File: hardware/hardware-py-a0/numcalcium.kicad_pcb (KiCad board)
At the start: 2 copper layers, 77.6 x 158.1 mm, 111 parts, among them J1 Conn_02x08_Odd_Even, J12 Micro_SD_Card_Det2, J2 USB_C_Receptacle_USB2.0_16P, J3 Conn_02x04_Odd_Even, J4 LCD_socket, J9 AudioJack4, Q1 AO3401A, Q2 AO3401A, Q3 AO3401A, Q6 BSS138, Q7 AO3401A, Q8 BSS138, Q9 BSS138, SW1 SW_Push, SW10 SW_Push, SW11 SW_Push, SW12 SW_Push, SW13 SW_Push, SW14 SW_Push, SW15 SW_Push, SW16 SW_Push, SW17 SW_Push, SW18 SW_Push, SW19 SW_Push, SW2 SW_Push, SW20 SW_Push, SW21 Encoder, SW22 RST, SW3 SW_Push, SW4 SW_Push, SW5 SW_Push, SW6 SW_Push, SW7 SW_Push, SW8 SW_Push, SW9 SW_Push, U1 LTC4054ES5-4.2, U2 STI3411A, U3 74HC595, U4 ESP32-S3-WROOM-1, U6 XC6206PxxxMR

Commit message: [dev] py-a0 board files
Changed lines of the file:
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@@
 		(tags "SOT TO_SOT_SMD")
 		(property "Reference" "U6"
-			(at -0.508 0 360)
+			(at -0.508 0 0)
 			(layer "F.SilkS")
 			(effects
@@
 		)
 		(property "Value" "XC6206PxxxMR"
-			(at 0 2.4 360)
+			(at 0 2.4 0)
 			(layer "F.Fab")
 			(effects
@@
 		)
 		(fp_text user "${REFERENCE}"
-			(at 0 0 360)
+			(at 0 0 0)
 			(layer "F.Fab")
 			(effects
@@
 		(tags "diode handsolder")
 		(property "Reference" "D24"
-			(at -0.009 0.0254 360)
+			(at -0.009 0.0254 0)
 			(layer "F.SilkS")
 			(effects
@@
 		(tags "SOT TO_SOT_SMD")
 		(property "Reference" "Q3"
-			(at -0.6835 0 360)
+			(at -0.6835 0 0)
 			(layer "F.SilkS")
 			(effects
@@
 		)
 		(property "Value" "AO3401A"
-			(at 0 2.4 360)
+			(at 0 2.4 0)
 			(layer "F.Fab")
 			(effects
@@
 		)
 		(fp_text user "${REFERENCE}"
-			(at 0 0 360)
+			(at 0 0 0)
 			(layer "F.Fab")
 			(effects
@@
 		)
 		(fp_text user "+"
-			(at -1.326 4.9836 360)
+			(at -1.326 4.9836 0)
 			(layer "B.SilkS")
 			(effects
@@
 		)
 		(fp_text user "+"
-			(at -2.75 2.75 360)
+			(at -2.75 2.75 0)
 			(layer "B.Fab")
 			(effects
@@
 		(tags "diode handsolder")
 		(property "Reference" "D27"
-			(at 0 -0.0254 360)
+			(at 0 -0.0254 0)
 			(layer "B.SilkS")
 			(effects
@@
 		(polygon
 			(pts
-				(xy -1.016 -35.56) (xy 33.528 -35.56) (xy 33.528 -27.432) (xy 57.912 -27.432) (xy 57.912 -3.048)
+				(xy -1.2192 -35.6108) (xy 33.528 -35.56) (xy 33.528 -27.432) (xy 57.912 -27.432) (xy 57.912 -3.048)
 				(xy -1.016 -3.048)
 			)

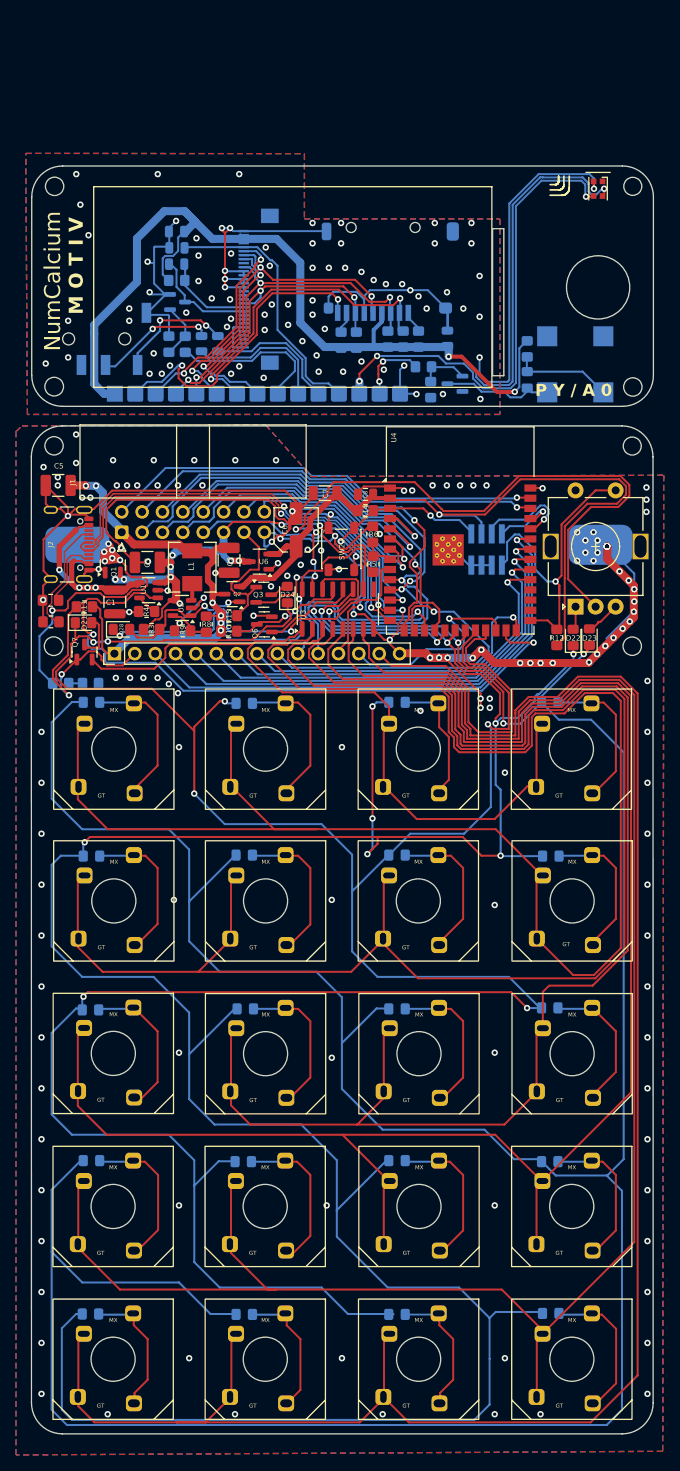
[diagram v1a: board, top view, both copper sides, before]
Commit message: hardware: py/a0 revision 1.1 using FFC connectors
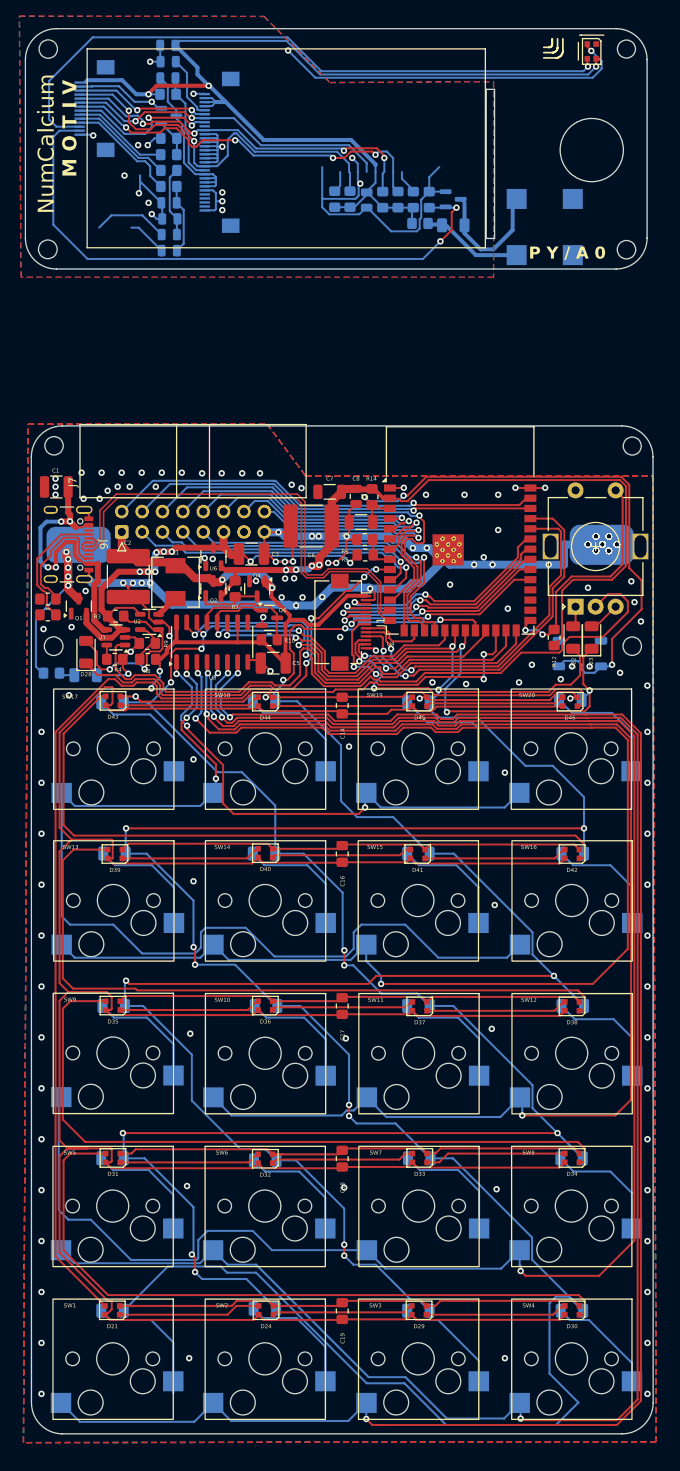
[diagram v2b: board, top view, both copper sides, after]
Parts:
- removed IPC1: Conn_01x16_Pin, Connector_PinHeader_2.54mm:PinHeader_1x15_P2.54mm_Vertical
- removed IPC2: Conn_01x16_Socket, footprints:PinSocket_1x15_P2.54mm_Vertical_Pads
- removed J12: Micro_SD_Card_Det2, footprints:microSD_Short_1
- removed J4: LCD_socket, Connector_FFC-FPC:Hirose_FH12-30S-0.5SH_1x30-1MP_P0.50mm_Horizontal
- removed J9: AudioJack4, footprints:Jack_3.5mm_PJ320D_Horizontal
- removed Q3, Q7: AO3401A, Package_TO_SOT_SMD:SOT-23
- removed R15: 100k, Resistor_SMD:R_0805_2012Metric_Pad1.20x1.40mm_HandSolder
- added C14: 1u, Capacitor_SMD:C_0805_2012Metric_Pad1.18x1.45mm_HandSolder, F.Cu at (38.2, 33.3)
- added C16: 1u, Capacitor_SMD:C_0805_2012Metric_Pad1.18x1.45mm_HandSolder, F.Cu at (38.2, 51.8)
- added C17: 1u, Capacitor_SMD:C_0805_2012Metric_Pad1.18x1.45mm_HandSolder, F.Cu at (38.2, 70.7)
- added C18: 1u, Capacitor_SMD:C_0805_2012Metric_Pad1.18x1.45mm_HandSolder, F.Cu at (38.2, 89.8)
- added C19: 1u, Capacitor_SMD:C_0805_2012Metric_Pad1.18x1.45mm_HandSolder, F.Cu at (38.2, 108.8)
- added C20: 470n, Capacitor_SMD:C_0805_2012Metric, B.Cu at (16.7, -27.4)
- added C21: 470n, Capacitor_SMD:C_0805_2012Metric, B.Cu at (16.6, -29.4)
- added C4: 1u, Capacitor_SMD:C_1206_3216Metric, F.Cu at (40.6, 10.4)
- added D29: WS2812B-2020, LED_SMD:LED_WS2812B-2020_PLCC4_2.0x2.0mm, F.Cu at (47.8, 108.7)
- added D30: WS2812B-2020, LED_SMD:LED_WS2812B-2020_PLCC4_2.0x2.0mm, F.Cu at (66.9, 108.7)
- added D31: WS2812B-2020, LED_SMD:LED_WS2812B-2020_PLCC4_2.0x2.0mm, F.Cu at (9.66, 89.7)
- added D32: WS2812B-2020, LED_SMD:LED_WS2812B-2020_PLCC4_2.0x2.0mm, F.Cu at (28.7, 89.8)
- added D33: WS2812B-2020, LED_SMD:LED_WS2812B-2020_PLCC4_2.0x2.0mm, F.Cu at (47.9, 89.7)
- added D34: WS2812B-2020, LED_SMD:LED_WS2812B-2020_PLCC4_2.0x2.0mm, F.Cu at (66.9, 89.7)
- added D35: WS2812B-2020, LED_SMD:LED_WS2812B-2020_PLCC4_2.0x2.0mm, F.Cu at (9.66, 70.7)
- added D36: WS2812B-2020, LED_SMD:LED_WS2812B-2020_PLCC4_2.0x2.0mm, F.Cu at (28.7, 70.7)
- added D37: WS2812B-2020, LED_SMD:LED_WS2812B-2020_PLCC4_2.0x2.0mm, F.Cu at (47.9, 70.8)
- added D38: WS2812B-2020, LED_SMD:LED_WS2812B-2020_PLCC4_2.0x2.0mm, F.Cu at (66.9, 70.8)
- added D39: WS2812B-2020, LED_SMD:LED_WS2812B-2020_PLCC4_2.0x2.0mm, F.Cu at (9.91, 51.8)
- added D40: WS2812B-2020, LED_SMD:LED_WS2812B-2020_PLCC4_2.0x2.0mm, F.Cu at (28.7, 51.7)
- added D41: WS2812B-2020, LED_SMD:LED_WS2812B-2020_PLCC4_2.0x2.0mm, F.Cu at (47.7, 51.8)
- added D42: WS2812B-2020, LED_SMD:LED_WS2812B-2020_PLCC4_2.0x2.0mm, F.Cu at (66.9, 51.8)
- added D43: WS2812B-2020, LED_SMD:LED_WS2812B-2020_PLCC4_2.0x2.0mm, F.Cu at (9.66, 32.7)
- added D44: WS2812B-2020, LED_SMD:LED_WS2812B-2020_PLCC4_2.0x2.0mm, F.Cu at (28.7, 32.8)
- added D45: WS2812B-2020, LED_SMD:LED_WS2812B-2020_PLCC4_2.0x2.0mm, F.Cu at (47.9, 32.8)
- added D46: WS2812B-2020, LED_SMD:LED_WS2812B-2020_PLCC4_2.0x2.0mm, F.Cu at (66.7, 32.8)
- added J6: USB_C_Receptacle_USB2.0_16P, Connector_USB:USB_C_Receptacle_GCT_USB4105-xx-A_16P_TopMnt_Horizontal, F.Cu at (2.97, 13.2)
- added J7: Conn_02x08_Odd_Even, footprints:IDC-Header_2x08_P2.54mm_Horizontal, F.Cu at (10.8, 11.6)
- added Q4: BSS138, Package_TO_SOT_SMD:SOT-23, F.Cu at (27.6, 18.7)
- added R7: 1M, Resistor_SMD:R_0805_2012Metric_Pad1.20x1.40mm_HandSolder, F.Cu at (24.9, 18.7)
- C2: value 22u -> 220u; footprint Resistor_SMD:R_1210_3225Metric_Pad1.30x2.65mm_HandSolder -> Capacitor_SMD:C_2220_5750Metric
- C6: footprint Capacitor_SMD:C_Elec_5x5.4 -> Capacitor_SMD:C_2220_5750Metric
- D1, D10, D11, D12, D13, D14, D15, D16, D17, D18, D19, D2, D20, D22, D23, D27, D28, D3, D4, D5, D6, D7, D8, D9: footprint Diode_SMD:D_0805_2012Metric_Pad1.15x1.40mm_HandSolder -> Diode_SMD:D_1206_3216Metric
- D21, D24: value D -> WS2812B-2020; footprint Diode_SMD:D_0805_2012Metric_Pad1.15x1.40mm_HandSolder -> LED_SMD:LED_WS2812B-2020_PLCC4_2.0x2.0mm
- D25: footprint Resistor_SMD:R_0805_2012Metric_Pad1.20x1.40mm_HandSolder -> Diode_SMD:D_1206_3216Metric
- J1: value Conn_02x08_Odd_Even -> Conn_01x14_Socket; footprint footprints:IDC-Header_2x08_P2.54mm_Horizontal -> Connector_FFC-FPC:Hirose_FH12-14S-0.5SH_1x14-1MP_P0.50mm_Horizontal
- J2: value USB_C_Receptacle_USB2.0_16P -> Conn_01x14_Socket; footprint Connector_USB:USB_C_Receptacle_GCT_USB4105-xx-A_16P_TopMnt_Horizontal -> Connector_FFC-FPC:Hirose_FH12-14S-0.5SH_1x14-1MP_P0.50mm_Horizontal; moved to B.Cu
- J3: value Conn_02x04_Odd_Even -> LCD_socket; footprint Connector_PinHeader_1.27mm:PinHeader_2x04_P1.27mm_Vertical_SMD -> Connector_FFC-FPC:Hirose_FH12-30S-0.5SH_1x30-1MP_P0.50mm_Horizontal
- R10: value 100k -> 1M
- R11: value 100k -> 100; moved to B.Cu
- R12: value 100k -> 470k
- R13: value 10k -> 100
- R14: value 100k -> 10k
- R16, R17: value 5k6 -> 5k1
- R27: value 10k -> 1M
- SW1, SW10, SW11, SW12, SW13, SW14, SW15, SW16, SW17, SW18, SW19, SW2, SW20, SW3, SW4, SW5, SW6, SW7, SW8, SW9: footprint footprints:Combo_MechanicalSwitch -> footprints:CherrySocket_MechanicalSwitch
- SW22: value RST -> SW_Push; moved to B.Cu
- moved D24 89.3 mm to (28.7, 108.7), turned to 180 degrees
- moved D21 85.8 mm to (9.58, 108.7), turned to 180 degrees
- moved J3 59.7 mm to (22.9, -35.7), turned to -90 degrees
- moved J2 54.5 mm to (7.34, -41.2)
- moved R11 53.5 mm to (16.6, -31.5)
- moved R13 40.1 mm to (16.6, -33.5), turned to 180 degrees
- moved C5 34.8 mm to (29.6, 28.0)
- moved SW22 32.5 mm to (67.9, 26.8), turned to 0 degrees
- moved J1 30.7 mm to (39.3, 22.9), turned to -90 degrees
- moved R18 25.7 mm to (16.6, -37.5), turned to 180 degrees
- moved R20 23.7 mm to (16.6, -35.4), turned to 0 degrees
- moved R27 23.7 mm to (49.1, -29.8), turned to 90 degrees
- moved C11 23.2 mm to (16.5, -47.0)
- moved Q9 23.2 mm to (16.6, -40.3)
- moved R19 23.2 mm to (16.5, -43.0)
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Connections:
- C12 pad 2: /Front/A_T -> Net-(C12-Pad2)
- C13 pad 2: /Front/A_R1 -> Net-(C13-Pad2)
- C9 pad 1: Net-(J4-Pin_21) -> Net-(J3-Pin_21)
- C9 pad 2: Net-(J4-Pin_20) -> Net-(J3-Pin_20)
- D21 pad 1: IO_T -> Net-(D21-DOUT)
- D21 pad 2: Net-(D21-A) -> GND
- D24 pad 1: IO_T -> Net-(D24-DOUT)
- D24 pad 2: Net-(D24-A) -> GND
- J1 pad 10: Net-(J1-Pin_10) -> /Main/AUD_R
- J1 pad 11: VBAT -> /Main/AUD_L
- J1 pad 12: Net-(J1-Pin_12) -> /Main/STATUS_LED
- J1 pad 13: CART_SENSE -> /Main/BUZ_DRIVE
- J1 pad 14: Net-(J1-Pin_14) -> GND
- J1 pad 2: Net-(J1-Pin_2) -> GND
- J1 pad 3: RX1 -> /Main/LCD_CS
- J1 pad 4: Net-(J1-Pin_4) -> /Main/MISO
- J1 pad 5: TX1 -> /Main/MOSI
- J1 pad 6: Net-(J1-Pin_6) -> /Main/CK
- J1 pad 7: Net-(J1-Pin_7) -> /Main/SD_CS
- J1 pad 8: Net-(J1-Pin_8) -> /Main/LCD_DC
- J1 pad 9: Net-(J1-Pin_9) -> /Main/LCD_LED
- J3 pad 1: #B_OK -> GND
- J3 pad 2: Net-(J3-Pin_2) -> /Front/VDD
- J3 pad 3: GND -> /Front/VDD
- J3 pad 4: Net-(J3-Pin_4) -> /Front/VDD
- J3 pad 5: GND -> /Front/LCD_RST
- J3 pad 6: VDD_AON -> /Front/LCD_CS
- J3 pad 7: GND -> /Front/CK
- J3 pad 8: RST -> /Front/LCD_DC
- Q2 pad 1: Net-(D28-A) -> Net-(Q2-G)
- Q8 pad 1: Net-(Q8-G) -> /Front/BUZZER
- Q9 pad 3: Net-(J4-Pin_21) -> Net-(J3-Pin_21)
- R11 pad 1: VDD -> Net-(C12-Pad2)
- R11 pad 2: /Main/SD_DET -> /Front/A_T
- R13 pad 1: /Front/BUZZER -> Net-(C13-Pad2)
- R13 pad 2: Net-(Q8-G) -> /Front/A_R1
- R14 pad 1: RST -> VDD_AON
- R14 pad 2: VDD_AON -> RST
- R16 pad 1: Net-(J2-CC2) -> Net-(J6-CC2)
- R17 pad 1: Net-(J2-CC1) -> Net-(J6-CC1)
- R19 pad 1: Net-(J4-Pin_20) -> Net-(J3-Pin_20)
- R27 pad 1: Net-(Q8-G) -> /Front/BUZZER
- SW1 pad 1: Net-(D1-A) -> Net-(U3-QH)
- SW1 pad 2: Net-(U3-QH) -> Net-(D1-A)
- SW10 pad 1: Net-(D10-A) -> Net-(U3-QE)
- SW10 pad 2: Net-(U3-QE) -> Net-(D10-A)
- SW11 pad 1: Net-(D11-A) -> Net-(U3-QE)
- SW11 pad 2: Net-(U3-QE) -> Net-(D11-A)
- SW12 pad 1: Net-(D12-A) -> Net-(U3-QE)
- SW12 pad 2: Net-(U3-QE) -> Net-(D12-A)
- SW13 pad 1: Net-(D13-A) -> Net-(U3-QD)
- SW13 pad 2: Net-(U3-QD) -> Net-(D13-A)
- SW14 pad 1: Net-(D14-A) -> Net-(U3-QD)
- SW14 pad 2: Net-(U3-QD) -> Net-(D14-A)
- SW15 pad 1: Net-(D15-A) -> Net-(U3-QD)
- SW15 pad 2: Net-(U3-QD) -> Net-(D15-A)
- SW16 pad 1: Net-(D16-A) -> Net-(U3-QC)
- SW16 pad 2: Net-(U3-QC) -> Net-(D16-A)
- SW17 pad 1: Net-(D17-A) -> Net-(U3-QC)
- SW17 pad 2: Net-(U3-QC) -> Net-(D17-A)
- SW18 pad 1: Net-(D18-A) -> Net-(U3-QC)
- SW18 pad 2: Net-(U3-QC) -> Net-(D18-A)
- SW19 pad 1: Net-(D19-A) -> Net-(U3-QB)
- SW19 pad 2: Net-(Q7-S) -> Net-(D19-A)
- SW2 pad 1: Net-(D2-A) -> Net-(U3-QH)
- SW2 pad 2: Net-(U3-QH) -> Net-(D2-A)
- SW20 pad 1: Net-(D20-A) -> Net-(U3-QB)
- SW20 pad 2: Net-(Q7-S) -> Net-(D20-A)
- SW3 pad 1: Net-(D3-A) -> Net-(U3-QH)
- SW3 pad 2: Net-(U3-QH) -> Net-(D3-A)
- SW4 pad 1: Net-(D4-A) -> Net-(U3-QG)
- SW4 pad 2: Net-(U3-QG) -> Net-(D4-A)
- SW5 pad 1: Net-(D5-A) -> Net-(U3-QG)
- SW5 pad 2: Net-(U3-QG) -> Net-(D5-A)
- SW6 pad 1: Net-(D6-A) -> Net-(U3-QG)
- SW6 pad 2: Net-(U3-QG) -> Net-(D6-A)
- SW7 pad 1: Net-(D7-A) -> Net-(U3-QF)
- SW7 pad 2: Net-(U3-QF) -> Net-(D7-A)
- SW8 pad 1: Net-(D8-A) -> Net-(U3-QF)
- SW8 pad 2: Net-(U3-QF) -> Net-(D8-A)
- SW9 pad 1: Net-(D9-A) -> Net-(U3-QF)
- SW9 pad 2: Net-(U3-QF) -> Net-(D9-A)
- U3 pad 1: Net-(Q7-S) -> Net-(U3-QB)
- U4 pad 12: Net-(J1-Pin_16) -> Net-(J7-Pin_16)
- U4 pad 15: Net-(J1-Pin_6) -> Net-(J7-Pin_6)
- U4 pad 17: Net-(J1-Pin_9) -> Net-(J7-Pin_9)
- U4 pad 18: Net-(J1-Pin_7) -> Net-(J7-Pin_7)
- U4 pad 24: /Main/STATUS_LED -> /Main/lighting/DIN
- U4 pad 36: Net-(J3-Pin_4) -> /Main/AUD_R
- U4 pad 37: Net-(J3-Pin_2) -> /Main/AUD_L
- U4 pad 38: Net-(J1-Pin_4) -> Net-(J7-Pin_4)
- U4 pad 39: Net-(J1-Pin_2) -> Net-(J7-Pin_2)
- U4 pad 4: Net-(J1-Pin_8) -> Net-(J7-Pin_8)
- U4 pad 5: Net-(J1-Pin_10) -> Net-(J7-Pin_10)
- U4 pad 6: Net-(J1-Pin_12) -> Net-(J7-Pin_12)
- U4 pad 7: Net-(J1-Pin_14) -> Net-(J7-Pin_14)
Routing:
- net VDD: track 97.8 -> 491.7 mm, vias 7 -> 4
- net GND: track 420.8 -> 605.2 mm, vias 240 -> 257
- net IO_D: track 421.8 -> 275.7 mm, vias 4 -> 13
- net /Main/lighting/DIN: track 0.00 -> 141.3 mm, vias 0 -> 2
- net IO_T: track 328.5 -> 213.6 mm
- net Net-(Q7-S): track 92.4 -> 0.00 mm
- net Net-(D38-DOUT): track 0.00 -> 89.2 mm
- net Net-(D34-DOUT): track 0.00 -> 88.4 mm
- net Net-(U3-QC): track 211.3 -> 123.4 mm, vias 0 -> 3
- net Net-(D42-DOUT): track 0.00 -> 86.9 mm
- net Net-(D30-DOUT): track 0.00 -> 86.8 mm
- net /Front/BUZZER: track 9.42 -> 74.1 mm
- net Net-(U3-QB): track 0.00 -> 61.9 mm, vias 0 -> 3
- net Net-(J1-Pin_2): track 54.9 -> 0.00 mm, vias 1 -> 0
- net Net-(J7-Pin_2): track 0.00 -> 54.5 mm, vias 0 -> 1
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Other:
- board size 77.6 x 158.1 mm -> 78.3 x 175.2 mm
- board text removed: "PROG"
- board text removed: "TRVR BGGG"

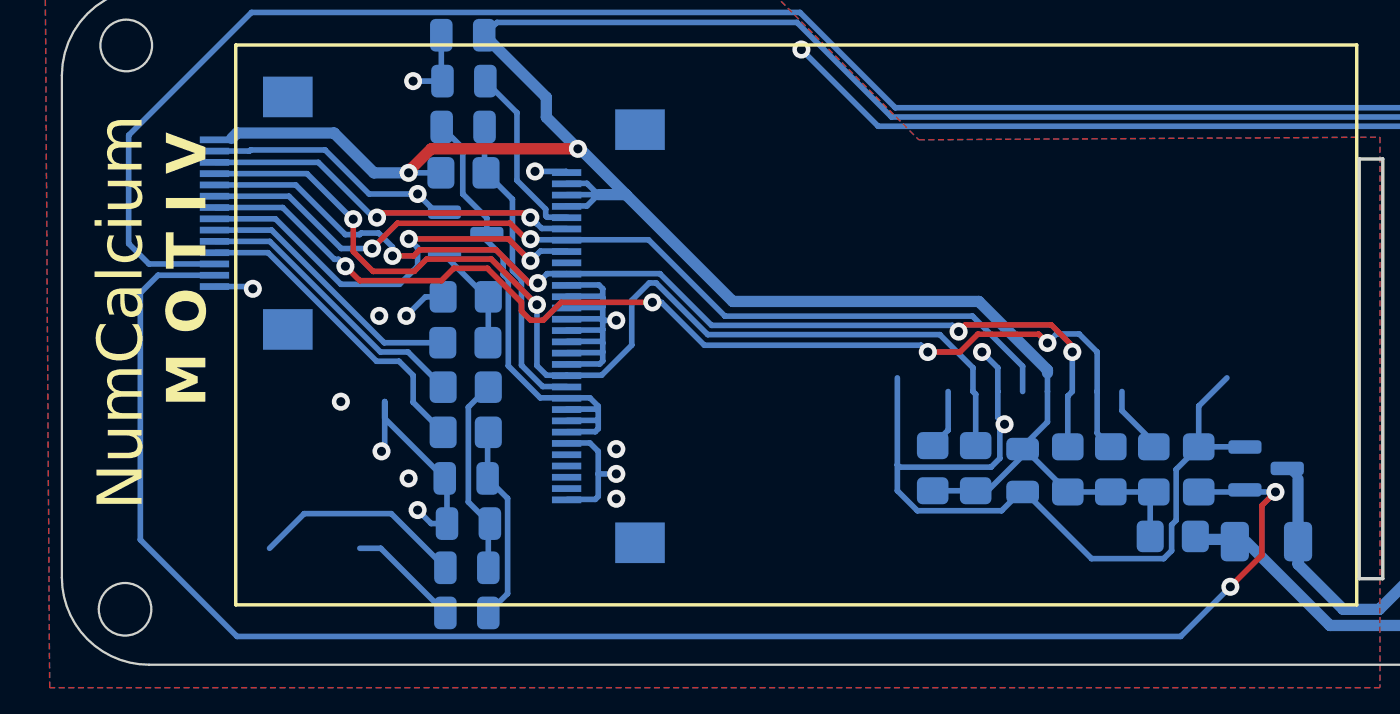
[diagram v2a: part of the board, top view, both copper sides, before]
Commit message: terminal:os.dupterm Stream support
move files and rename folders to board_src and scripts
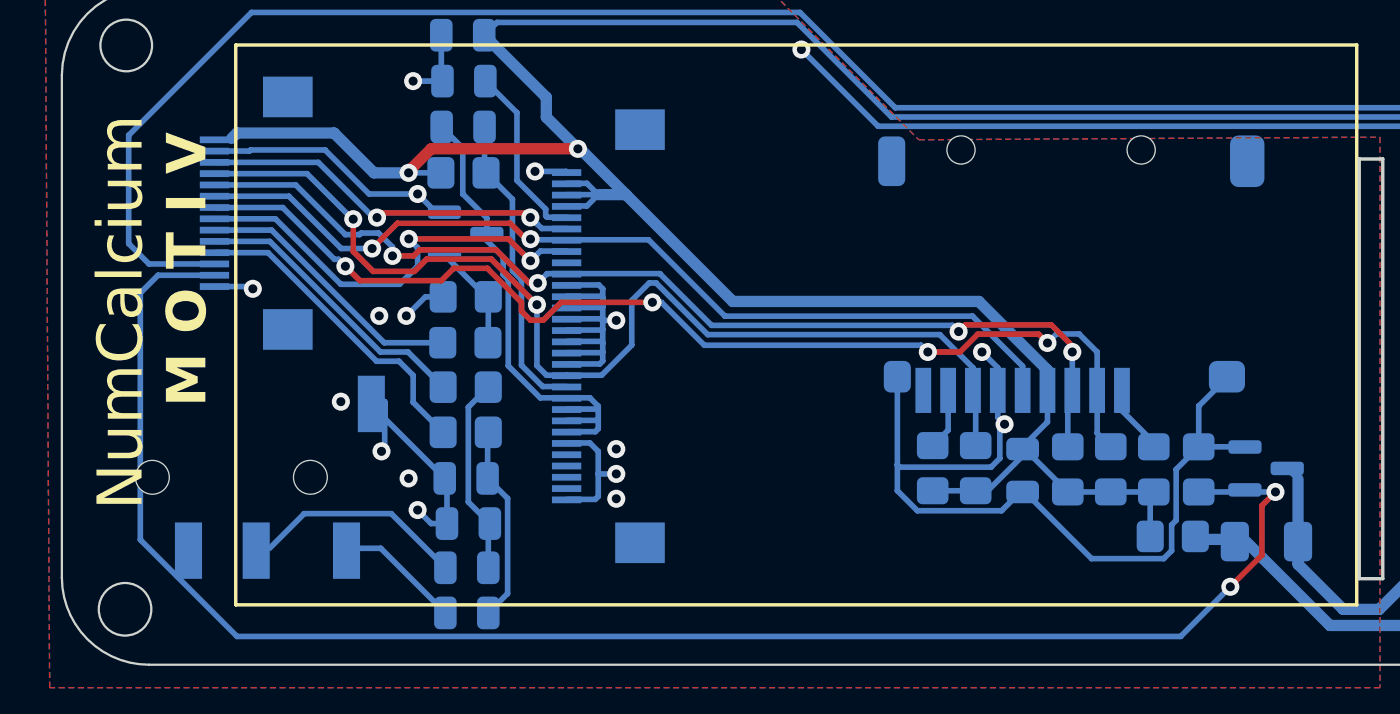
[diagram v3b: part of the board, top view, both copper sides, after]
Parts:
- added J4: Micro_SD_Card_Det2, footprints:microSD_Short_1, B.Cu at (43.5, -40.0)
- added J5: AudioJack4, footprints:Jack_3.5mm_PJ320D_Horizontal, B.Cu at (7.52, -29.5)
- R11, R13: value 100 -> 22
